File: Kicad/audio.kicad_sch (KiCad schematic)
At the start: 70 parts, among them J701 Conn_01x04, J702 Conn_02x05, J703 Conn_01x04, U701 TLV320AIC23BPW, U702 STX-4335-5BGP-S1, Y701 12M 20pF

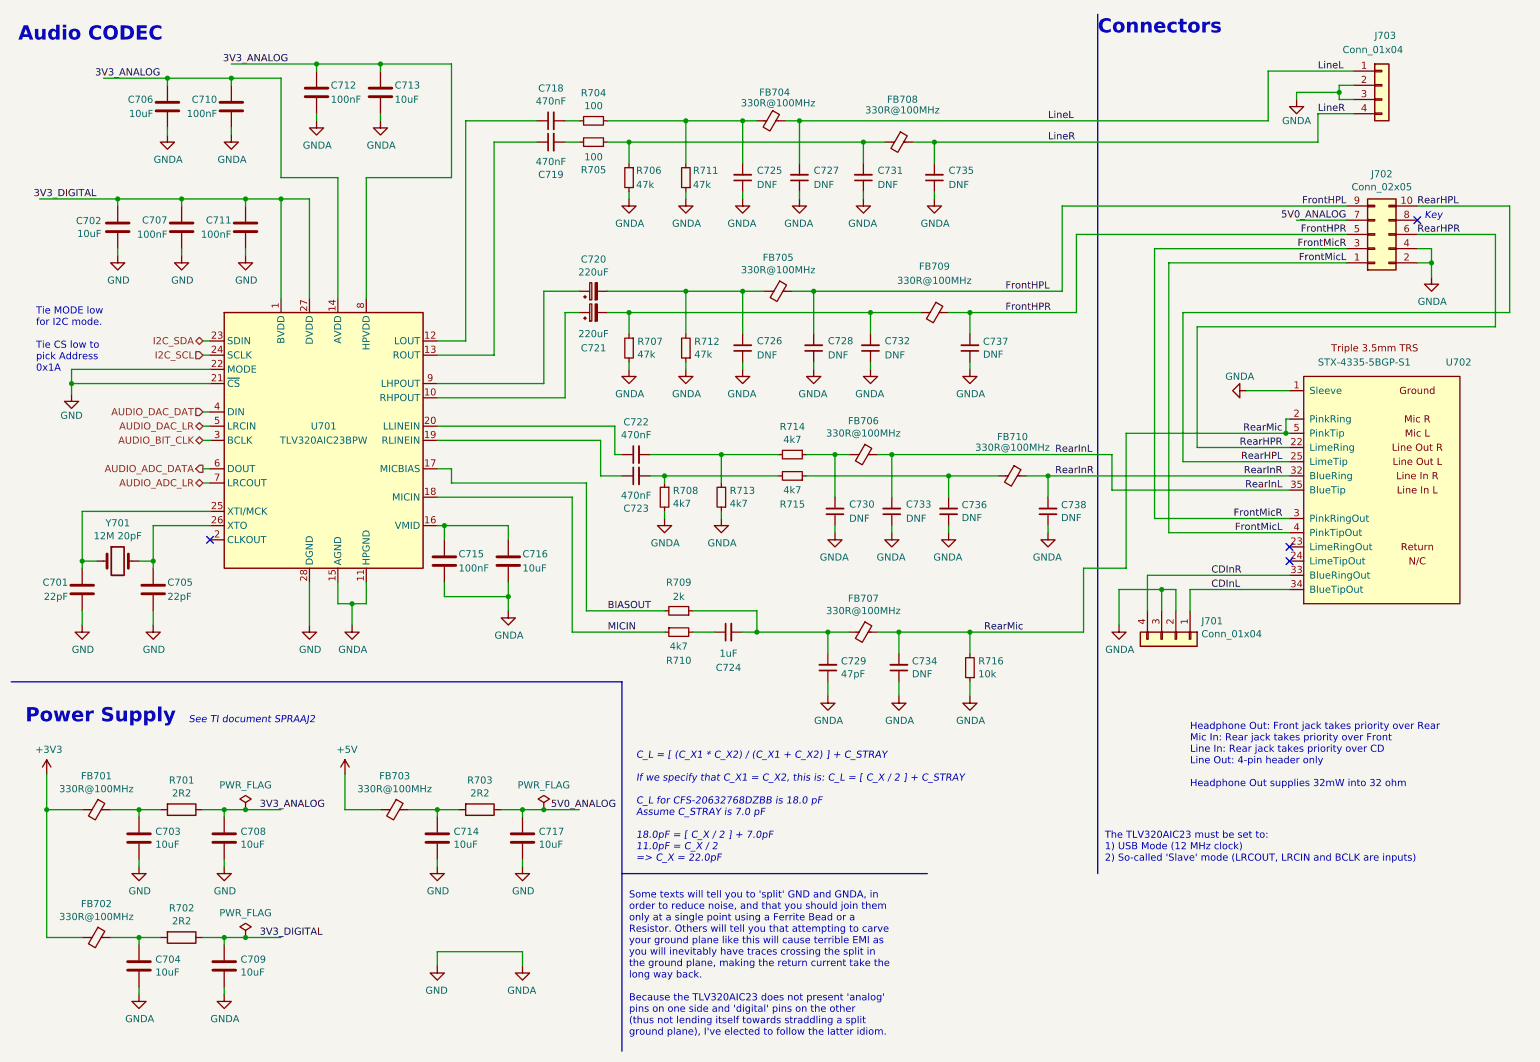
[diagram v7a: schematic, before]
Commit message: Reworked audio circuit.
Based on TLV320AIC23B evaluation board. Removed Pi filters. Used SMD
electrolytic caps for headphone out.
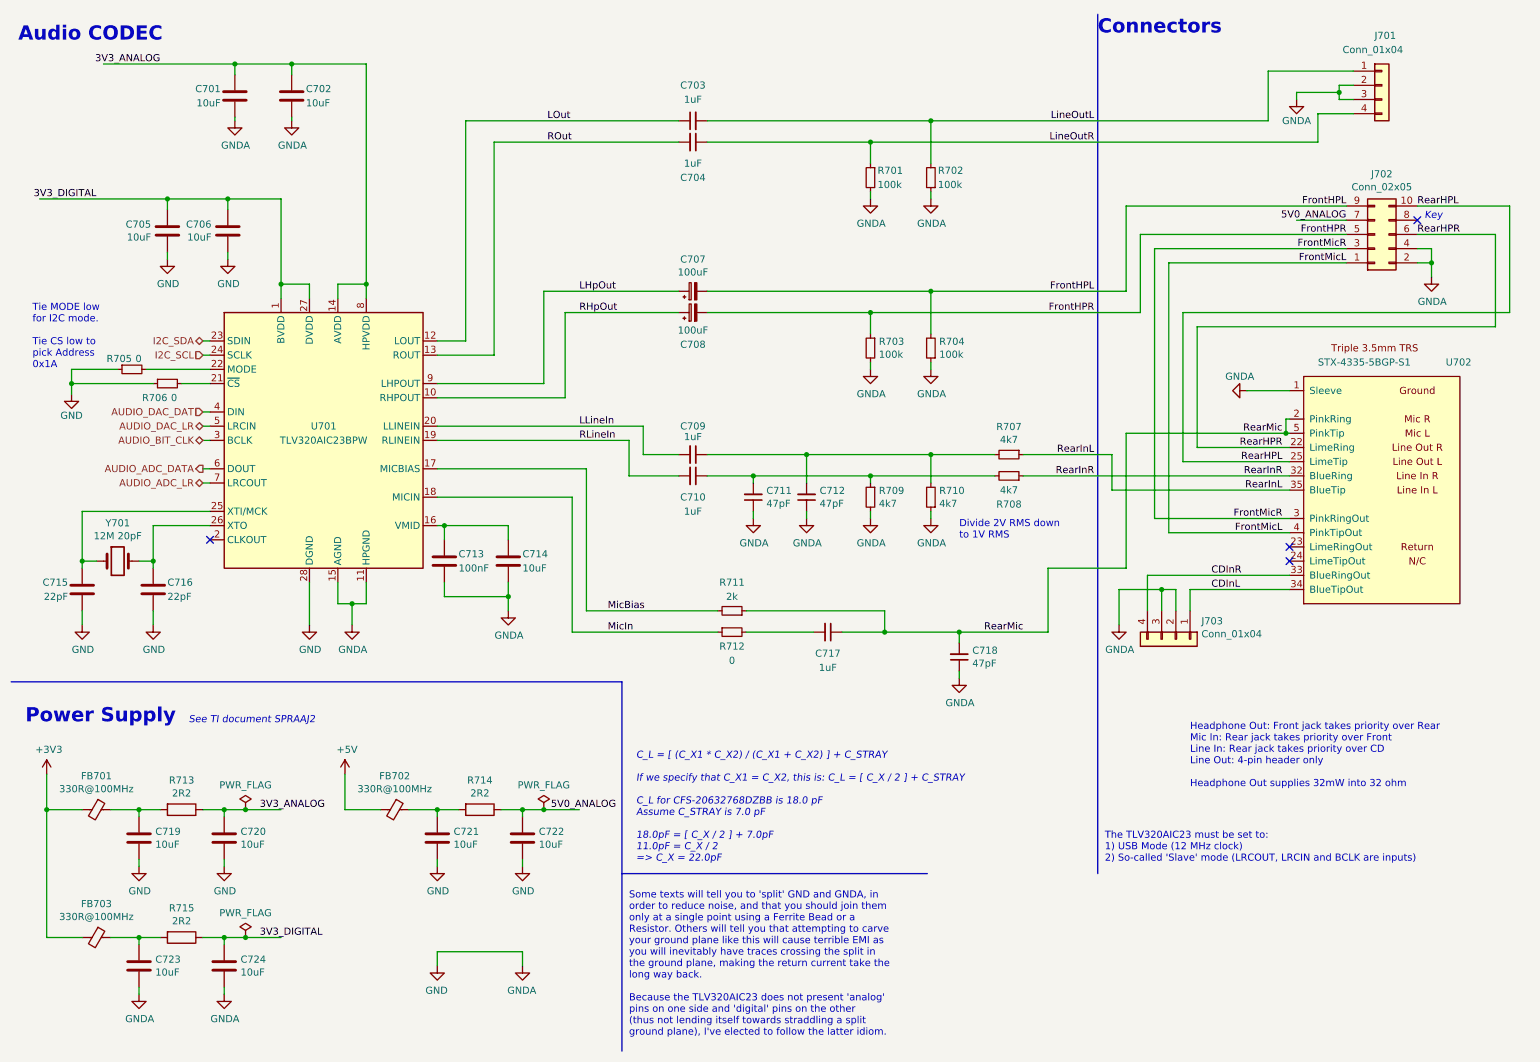
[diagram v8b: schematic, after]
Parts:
- removed C707, C710, C711, C712: 100nF, Capacitor_SMD:C_0805_2012Metric_Pad1.18x1.45mm_HandSolder, symbol Device:C
- removed C718, C719, C722, C723: 470nF, Capacitor_SMD:C_0805_2012Metric_Pad1.18x1.45mm_HandSolder, symbol Device:C_Small
- removed C721: 220uF, Capacitor_THT:CP_Radial_D8.0mm_P5.00mm, symbol Device:C_Polarized_Small
- removed C724: 1uF, Capacitor_SMD:C_0805_2012Metric_Pad1.18x1.45mm_HandSolder, symbol Device:C_Small
- removed C725, C726, C727, C728, C730, C731, C732, C733, C734, C735, C736, C737, C738: DNF, Capacitor_SMD:C_0805_2012Metric_Pad1.18x1.45mm_HandSolder, symbol Device:C_Small
- removed FB704, FB705, FB706, FB707, FB708, FB709, FB710: 330R@100MHz, Inductor_SMD:L_0805_2012Metric_Pad1.15x1.40mm_HandSolder, symbol Device:FerriteBead_Small
- removed R704: 100, Resistor_SMD:R_0805_2012Metric_Pad1.20x1.40mm_HandSolder, symbol Device:R_Small
- removed R716: 10k, Resistor_SMD:R_0805_2012Metric_Pad1.20x1.40mm_HandSolder, symbol Device:R_Small
- added C703, C704, C709, C710, C717: 1uF, Capacitor_SMD:C_0805_2012Metric_Pad1.18x1.45mm_HandSolder, symbol Device:C_Small
- added C706: 10uF, Capacitor_SMD:C_0805_2012Metric_Pad1.18x1.45mm_HandSolder, symbol Device:C
- added C708: 100uF, Capacitor_SMD:C_Elec_6.3x5.4, symbol Device:C_Polarized_Small
- added C711, C712: 47pF, Capacitor_SMD:C_0805_2012Metric_Pad1.18x1.45mm_HandSolder, symbol Device:C_Small
- added R706: 0, Resistor_SMD:R_0805_2012Metric_Pad1.20x1.40mm_HandSolder, symbol Device:R_Small
- C707: renamed from C720; value 220uF -> 100uF; footprint Capacitor_THT:CP_Radial_D8.0mm_P5.00mm -> Capacitor_SMD:C_Elec_6.3x5.4; Digikey P5183-ND -> (none); JLCPCB Collection (none) -> Extended; LCSC Part# (none) -> C111600; MPN ECA-1HM221 -> UWX1C101MCL1GB; Manufacturer Panasonic -> Nichicon; Mouser 667-ECA-1HM221 -> (none); Voltage 6.3V -> 16V
- R701: renamed from R706; value 47k -> 100k; LCSC Part# C17713 -> C149504; MPN 0805W8F4702T5E -> 0805W8F1003T5E
- R702: renamed from R711; value 47k -> 100k; LCSC Part# C17713 -> C149504; MPN 0805W8F4702T5E -> 0805W8F1003T5E
- R703: renamed from R707; value 47k -> 100k; LCSC Part# C17713 -> C149504; MPN 0805W8F4702T5E -> 0805W8F1003T5E
- R704: renamed from R712; value 47k -> 100k; LCSC Part# C17713 -> C149504; MPN 0805W8F4702T5E -> 0805W8F1003T5E
- R705: value 100 -> 0; LCSC Part# C17408 -> C17477; MPN 0805W8F1000T5E -> 0805W8F0000T5E
- R712: renamed from R710; value 4k7 -> 0; LCSC Part# C17673 -> C17477; MPN 0805W8F4701T5E -> 0805W8F0000T5E
- renumbered C706 to C701, C713 to C702, C702 to C705, C715 to C713, C716 to C714, C701 to C715, C705 to C716, C729 to C718, C703 to C719, C708 to C720, C714 to C721, C717 to C722, C704 to C723, C709 to C724, FB703 to FB702, FB702 to FB703, J703 to J701, J701 to J703, R714 to R707, R715 to R708, R708 to R709, R713 to R710, R709 to R711, R701 to R713, R703 to R714, R702 to R715
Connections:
- net LineL is gone; now on net LineOutL: J701.1 (Pin_1)
- net LineR is gone; now on net LineOutR: J701.4 (Pin_4)
- net 3V3_DIGITAL: now also C706.1
- net FrontHPL: now also C707.2, R704.2
- net FrontHPR: now also R703.1, C708.2
- net GND: now also R705.1, C706.2, C711.1, C712.1, R706.1; no longer U701.21 (~{CS}), U701.22 (MODE)
- net RearInL: now also R707.1
- net RearInR: now also R708.1
- net RearMic: now also C718.2, R711.1, C717.1
- net RHpOut: now reaches U701.10 (RHPOUT)
- net RHpOut: now also C708.1
- net LOut: now reaches U701.12 (LOUT)
- net LOut: now also C703.1
- net ROut: now reaches U701.13 (ROUT)
- net ROut: now also C704.2
- net RLineIn: now reaches U701.19 (RLINEIN)
- net RLineIn: now also C710.2
- net LLineIn: now reaches U701.20 (LLINEIN)
- net LLineIn: now also C709.2
- net LHpOut: now reaches C707.1, U701.9 (LHPOUT)
- net LineOutL: now reaches R702.2
- net LineOutL: now also C703.2
- net at R705.2: now also U701.22 (MODE)
- net LineOutR: now reaches R701.1
- net LineOutR: now also C704.1; no longer R705.1
- net at R707.2, R710.2: now also C709.1, C712.2
- net at R708.2, R709.1: now also C710.1, C711.2
- net at R712.2: now also C717.2
- net BIASOUT renamed MicBias
- net MICIN renamed MicIn
- new net: R706.2, U701.21 (~{CS})
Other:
- note added: "Divide 2V RMS down to 1V RMS"
- moved on the sheet: C701, C702, C705, C707, C718, R701, R702, R703, R704, R707, R708, R709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
